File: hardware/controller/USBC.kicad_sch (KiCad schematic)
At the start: 8 parts

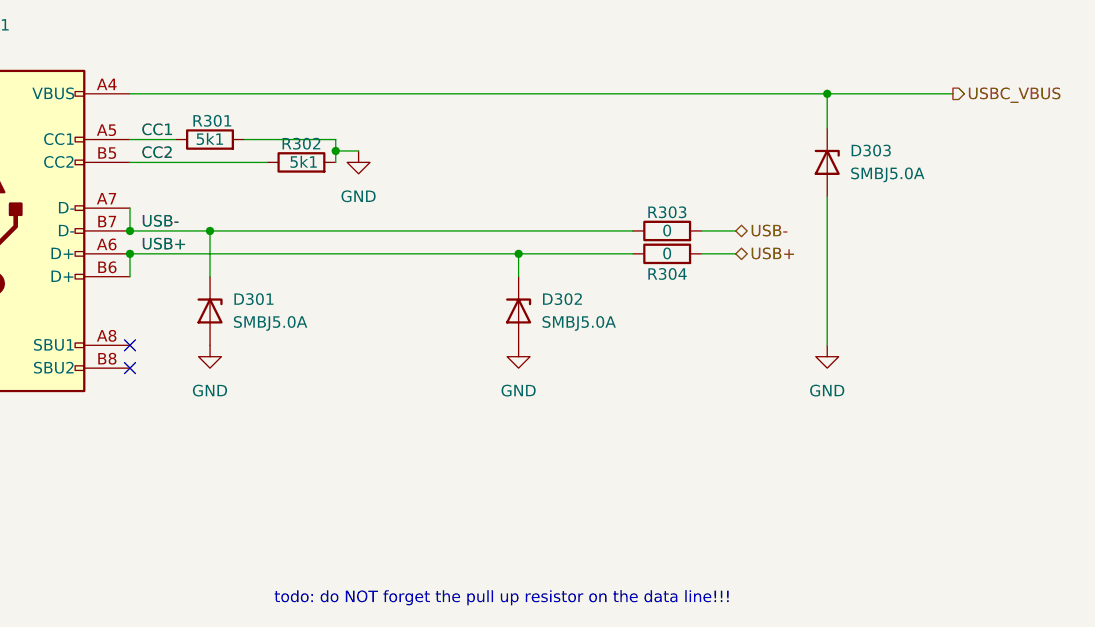
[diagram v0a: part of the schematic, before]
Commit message: fixed 3d models. rounded edges of pcb
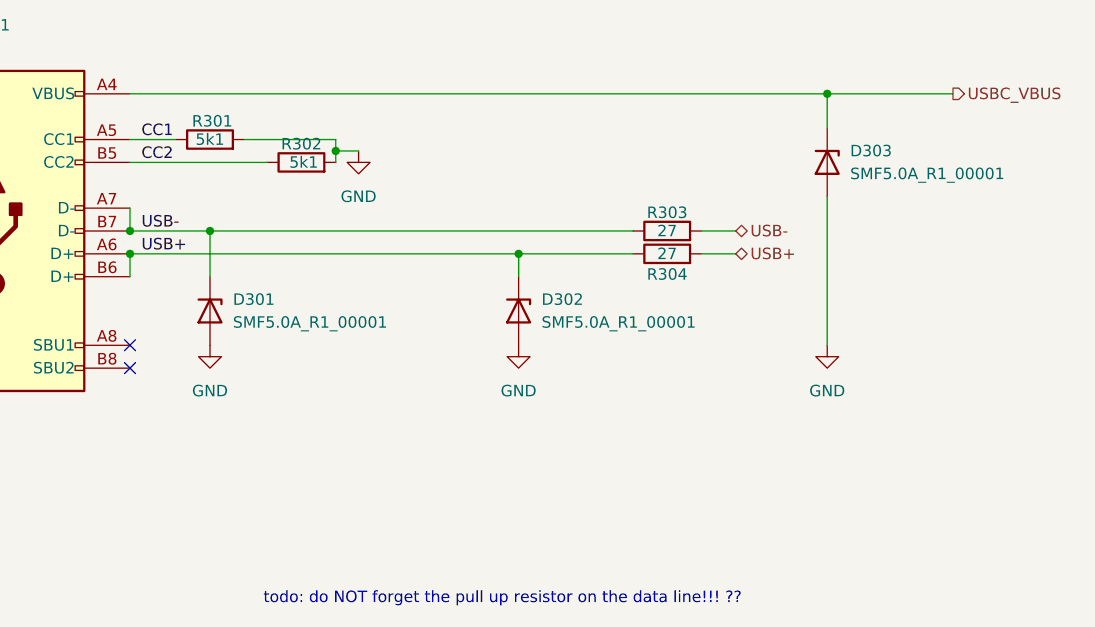
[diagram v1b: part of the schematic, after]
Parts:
- D301, D302, D303: value SMBJ5.0A -> SMF5.0A_R1_00001; footprint SamacSys_Parts:DIOM5436X261N -> SMF50A_R1_00001; Height 2.61 -> 1.1; Manufacturer_Name LITTELFUSE -> PANJIT; Manufacturer_Part_Number SMBJ5.0A -> SMF5.0A_R1_00001; Mouser Part Number 576-SMBJ5.0A -> 241-SMF5.0A_R1_00001; Mouser Price/Stock https://www.mouser.co.uk/ProductDetail/Littelfuse/SMBJ5.0A?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 -> https://www.mouser.co.uk/ProductDetail/Panjit/SMF5.0A_R1_00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
- R303, R304: value 0 -> 27; footprint SamacSys_Parts:RESC1608X50N -> RESC3216X65N; Height 0.5 -> 0.65; Manufacturer_Name Vishay -> ROHM Semiconductor; Manufacturer_Part_Number CRCW06030000Z0EA -> KTR18EZPF27R0; Mouser Part Number 71-CRCW0603-0-E3 -> 755-KTR18EZPF27R0; Mouser Price/Stock https://www.mouser.co.uk/ProductDetail/Vishay-Dale/CRCW0603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 -> https://www.mouser.com/Search/Refine.aspx?Keyword=755-KTR18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
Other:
- note added: "todo: do NOT forget the pull up resistor on the data line!!! ??"
- note removed: "todo: do NOT forget the pull up resistor on the data line!!!"
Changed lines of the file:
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@@
 	(generator_version "9.0")
 	(paper "A4")
-	(text "todo: do NOT forget the pull up resistor on the data line!!!"
+	(text "todo: do NOT forget the pull up resistor on the data line!!! ??"
 		(exclude_from_sim no)
 		(at 162.052 125.984 0)
@@
 			)
 		)
-		(property "Value" "SMBJ5.0A"
+		(property "Value" "SMF5.0A_R1_00001"
 			(at 166.37 95.2499 90)
 			(effects
@@
 			)
 		)
-		(property "Footprint" "SamacSys_Parts:DIOM5436X261N"
+		(property "Footprint" "SMF50A_R1_00001"
 			(at 70.18 104.14 0)
 			(effects
@@
 			)
 		)
-		(property "Datasheet" "https://www.mouser.co.uk/datasheet/2/240/Littelfuse_TVS_Diode_SMBJ_Datasheet.pdf-1108540.pdf"
+		(property "Datasheet" "https://www.mouser.in/datasheet/2/1057/SMF5.0A_SERIES-1868418.pdf"
 			(at -29.82 104.14 0)
 			(effects
@@
 			)
 		)
-		(property "Description" "Littelfuse SMBJ5.0A, Uni-Directional TVS Diode, 600W, 2-Pin DO-214AA"
+		(property "Description" "ESD Suppressors / TVS Diodes 200W,Transient Voltage Suppressors,SOD-123FL,5V,UNI"
 			(at 163.83 93.98 0)
 			(effects
@@
 			)
 		)
-		(property "Height" "2.61"
+		(property "Height" "1.1"
 			(at -229.82 104.14 0)
 			(effects
@@
 			)
 		)
-		(property "Mouser Part Number" "576-SMBJ5.0A"
+		(property "Mouser Part Number" "241-SMF5.0A_R1_00001"
 			(at -329.82 104.14 0)
 			(effects
@@
 			)
 		)
-		(property "Mouser Price/Stock" "https://www.mouser.co.uk/ProductDetail/Littelfuse/SMBJ5.0A?qs=JJML70Qc14t9tktzNr1oMQ%3D%3D"
+		(property "Mouser Price/Stock" "https://www.mouser.co.uk/ProductDetail/Panjit/SMF5.0A_R1_00001?qs=sPbYRqrBIVlx%2FHVv%252BUyL%252BQ%3D%3D"
 			(at -429.82 104.14 0)
 			(effects
@@
 			)
 		)
-		(property "Manufacturer_Name" "LITTELFUSE"
+		(property "Manufacturer_Name" "PANJIT"
 			(at -529.82 104.14 0)
 			(effects
@@
 			)
 		)
-		(property "Manufacturer_Part_Number" "SMBJ5.0A"
+		(property "Manufacturer_Part_Number" "SMF5.0A_R1_00001"
 			(at -629.82 104.14 0)
 			(effects
@@
 			)
 		)
-		(property "Value" "SMBJ5.0A"
+		(property "Value" "SMF5.0A_R1_00001"
 			(at 200.66 78.7399 90)
 			(effects
@@
 			)
 		)
-		(property "Footprint" "SamacSys_Parts:DIOM5436X261N"
+		(property "Footprint" "SMF50A_R1_00001"
 			(at 104.47 87.63 0)
 			(effects
@@
 			)
 		)
-		(property "Datasheet" "https://www.mouser.co.uk/datasheet/2/240/Littelfuse_TVS_Diode_SMBJ_Datasheet.pdf-1108540.pdf"
+		(property "Datasheet" "https://www.mouser.in/datasheet/2/1057/SMF5.0A_SERIES-1868418.pdf"
 			(at 4.47 87.63 0)
 			(effects
@@
 			)
 		)
-		(property "Description" "Littelfuse SMBJ5.0A, Uni-Directional TVS Diode, 600W, 2-Pin DO-214AA"
+		(property "Description" "ESD Suppressors / TVS Diodes 200W,Transient Voltage Suppressors,SOD-123FL,5V,UNI"
 			(at 198.12 77.47 0)
 			(effects
@@
 			)
 		)
-		(property "Height" "2.61"
+		(property "Height" "1.1"
 			(at -195.53 87.63 0)
 			(effects
@@
 			)
 		)
-		(property "Mouser Part Number" "576-SMBJ5.0A"
+		(property "Mouser Part Number" "241-SMF5.0A_R1_00001"
 			(at -295.53 87.63 0)
 			(effects
@@
 			)
 		)
-		(property "Mouser Price/Stock" "https://www.mouser.co.uk/ProductDetail/Littelfuse/SMBJ5.0A?qs=JJML70Qc14t9tktzNr1oMQ%3D%3D"
+		(property "Mouser Price/Stock" "https://www.mouser.co.uk/ProductDetail/Panjit/SMF5.0A_R1_00001?qs=sPbYRqrBIVlx%2FHVv%252BUyL%252BQ%3D%3D"
 			(at -395.53 87.63 0)
 			(effects
@@
 			)
 		)
-		(property "Manufacturer_Name" "LITTELFUSE"
+		(property "Manufacturer_Name" "PANJIT"
 			(at -495.53 87.63 0)
 			(effects
@@
 			)
 		)
-		(property "Manufacturer_Part_Number" "SMBJ5.0A"
+		(property "Manufacturer_Part_Number" "SMF5.0A_R1_00001"
 			(at -595.53 87.63 0)
 			(effects
@@
 			)
 		)
-		(property "Value" "0"
+		(property "Value" "27"
 			(at 180.34 87.63 90)
 			(effects
@@
 			)
 		)
-		(property "Footprint" "SamacSys_Parts:RESC1608X50N"
+		(property "Footprint" "RESC3216X65N"
 			(at 276.53 73.66 0)
 			(effects
@@
 			)
 		)
-		(property "Datasheet" "http://www.vishay.com/docs/20035/dcrcwe3.pdf"
+		(property "Datasheet" "https://componentsearchengine.com/Datasheets/1/KTR18EZPF27R0.pdf"
 			(at 376.53 73.66 0)
 			(effects
@@
 			)
 		)
-		(property "Description" "VISHAY - CRCW06030000Z0EA - RESISTOR, 0R, 0.1W, JUMPER, 0603, SMD"
+		(property "Description" "Thick Film Resistors - SMD 1206 27ohm 1% High VoltageAEC-Q200"
 			(at 180.34 87.63 0)
 			(effects
@@
 			)
 		)
-		(property "Height" "0.5"
+		(property "Height" "0.65"
 			(at 576.53 73.66 0)
 			(effects
@@
 			)
 		)
-		(property "Mouser Part Number" "71-CRCW0603-0-E3"
+		(property "Mouser Part Number" "755-KTR18EZPF27R0"
 			(at 676.53 73.66 0)
 			(effects
@@
 			)
 		)
-		(property "Mouser Price/Stock" "https://www.mouser.co.uk/ProductDetail/Vishay-Dale/CRCW06030000Z0EA?qs=uFJqmf%2F3rbbVtxvMdbYUaQ%3D%3D"
+		(property "Mouser Price/Stock" "https://www.mouser.com/Search/Refine.aspx?Keyword=755-KTR18EZPF27R0"
 			(at 776.53 73.66 0)
 			(effects
@@
 			)
 		)
-		(property "Manufacturer_Name" "Vishay"
+		(property "Manufacturer_Name" "ROHM Semiconductor"
 			(at 876.53 73.66 0)
 			(effects
@@
 			)
 		)
-		(property "Manufacturer_Part_Number" "CRCW06030000Z0EA"
+		(property "Manufacturer_Part_Number" "KTR18EZPF27R0"
 			(at 976.53 73.66 0)
 			(effects
@@
 			)
 		)
-		(property "Value" "SMBJ5.0A"
+		(property "Value" "SMF5.0A_R1_00001"
 			(at 132.08 95.2499 90)
 			(effects
@@
 			)
 		)
-		(property "Footprint" "SamacSys_Parts:DIOM5436X261N"
+		(property "Footprint" "SMF50A_R1_00001"
 			(at 35.89 104.14 0)
 			(effects
@@
 			)
 		)
-		(property "Datasheet" "https://www.mouser.co.uk/datasheet/2/240/Littelfuse_TVS_Diode_SMBJ_Datasheet.pdf-1108540.pdf"
+		(property "Datasheet" "https://www.mouser.in/datasheet/2/1057/SMF5.0A_SERIES-1868418.pdf"
 			(at -64.11 104.14 0)
 			(effects
@@
 			)
 		)
-		(property "Description" "Littelfuse SMBJ5.0A, Uni-Directional TVS Diode, 600W, 2-Pin DO-214AA"
+		(property "Description" "ESD Suppressors / TVS Diodes 200W,Transient Voltage Suppressors,SOD-123FL,5V,UNI"
 			(at 129.54 93.98 0)
 			(effects
@@
 			)
 		)
-		(property "Height" "2.61"
+		(property "Height" "1.1"
 			(at -264.11 104.14 0)
 			(effects
@@
 			)
 		)
-		(property "Mouser Part Number" "576-SMBJ5.0A"
+		(property "Mouser Part Number" "241-SMF5.0A_R1_00001"
 			(at -364.11 104.14 0)
 			(effects
@@
 			)
 		)
-		(property "Mouser Price/Stock" "https://www.mouser.co.uk/ProductDetail/Littelfuse/SMBJ5.0A?qs=JJML70Qc14t9tktzNr1oMQ%3D%3D"
+		(property "Mouser Price/Stock" "https://www.mouser.co.uk/ProductDetail/Panjit/SMF5.0A_R1_00001?qs=sPbYRqrBIVlx%2FHVv%252BUyL%252BQ%3D%3D"
 			(at -464.11 104.14 0)
 			(effects
@@
 			)
 		)
-		(property "Manufacturer_Name" "LITTELFUSE"
+		(property "Manufacturer_Name" "PANJIT"
 			(at -564.11 104.14 0)
 			(effects
@@
 			)
 		)
-		(property "Manufacturer_Part_Number" "SMBJ5.0A"
+		(property "Manufacturer_Part_Number" "SMF5.0A_R1_00001"
 			(at -664.11 104.14 0)
 			(effects
@@
 			)
 		)
-		(property "Value" "0"
+		(property "Value" "27"
 			(at 180.34 85.09 90)
 			(effects
@@
 			)
 		)
-		(property "Footprint" "SamacSys_Parts:RESC1608X50N"
+		(property "Footprint" "RESC3216X65N"
 			(at 276.53 71.12 0)
 			(effects
@@
 			)
 		)
-		(property "Datasheet" "http://www.vishay.com/docs/20035/dcrcwe3.pdf"
+		(property "Datasheet" "https://componentsearchengine.com/Datasheets/1/KTR18EZPF27R0.pdf"
 			(at 376.53 71.12 0)
 			(effects
@@
 			)
 		)
-		(property "Description" "VISHAY - CRCW06030000Z0EA - RESISTOR, 0R, 0.1W, JUMPER, 0603, SMD"
+		(property "Description" "Thick Film Resistors - SMD 1206 27ohm 1% High VoltageAEC-Q200"
 			(at 180.34 85.09 0)
 			(effects
@@
 			)
 		)
-		(property "Height" "0.5"
+		(property "Height" "0.65"
 			(at 576.53 71.12 0)
 			(effects
@@
 			)
 		)
-		(property "Mouser Part Number" "71-CRCW0603-0-E3"
+		(property "Mouser Part Number" "755-KTR18EZPF27R0"
 			(at 676.53 71.12 0)
 			(effects
@@
 			)
 		)
-		(property "Mouser Price/Stock" "https://www.mouser.co.uk/ProductDetail/Vishay-Dale/CRCW06030000Z0EA?qs=uFJqmf%2F3rbbVtxvMdbYUaQ%3D%3D"
+		(property "Mouser Price/Stock" "https://www.mouser.com/Search/Refine.aspx?Keyword=755-KTR18EZPF27R0"
 			(at 776.53 71.12 0)
 			(effects
@@
 			)
 		)
-		(property "Manufacturer_Name" "Vishay"
+		(property "Manufacturer_Name" "ROHM Semiconductor"
 			(at 876.53 71.12 0)
 			(effects
@@
 			)
 		)
-		(property "Manufacturer_Part_Number" "CRCW06030000Z0EA"
+		(property "Manufacturer_Part_Number" "KTR18EZPF27R0"
 			(at 976.53 71.12 0)
 			(effects

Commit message: man im tired
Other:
- note added: "todo: find smaller resistors that have pads to fit right into the USB data tracks"
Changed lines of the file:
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@@
+		)
+	)
+	(text "todo: find smaller resistors that have pads to fit right into\nthe USB data tracks"
+		(exclude_from_sim no)
+		(at 178.054 79.502 0)
+		(effects
+			(font
+				(size 1.27 1.27)
+			)
 		)
 	)

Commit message: a
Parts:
- D301, D302, D303: footprint SMF50A_R1_00001 -> SamacSys_Parts:SMF50A_R1_00001
- R303, R304: footprint RESC3216X65N -> SamacSys_Parts:RESC1005X40N; Height 0.65 -> 0.4; Manufacturer_Name ROHM Semiconductor -> Vishay; Manufacturer_Part_Number KTR18EZPF27R0 -> CRCW040227R0JNTD; Mouser Part Number 755-KTR18EZPF27R0 -> 71-CRCW0402J-27; Mouser Price/Stock https://www.mouser.com/Search/Refine.aspx?Keyword=755-KTR18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 -> https://www.mouser.com/Search/Refine.aspx?Keyword=71-CRCW04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
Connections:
- net USB+: no longer D302.1 (K), J301.A6 (D+), J301.B6 (D+), R304.1
- net USB-: no longer D301.1 (K), J301.A7 (D-), J301.B7 (D-), R303.1
- new net D+: D302.1 (K), J301.A6 (D+), J301.B6 (D+), R304.1
- new net D-: D301.1 (K), J301.A7 (D-), J301.B7 (D-), R303.1
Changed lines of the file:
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@@
 		)
 	)
-	(label "USB+"
+	(label "D+"
 		(at 121.92 87.63 0)
 		(effects
@@
 		)
 	)
-	(label "USB-"
+	(label "D-"
 		(at 121.92 85.09 0)
 		(effects
@@
 			)
 		)
-		(property "Footprint" "SMF50A_R1_00001"
+		(property "Footprint" "SamacSys_Parts:SMF50A_R1_00001"
 			(at 70.18 104.14 0)
 			(effects
@@
 			)
 		)
-		(property "Footprint" "SMF50A_R1_00001"
+		(property "Footprint" "SamacSys_Parts:SMF50A_R1_00001"
 			(at 104.47 87.63 0)
 			(effects
@@
 			)
 		)
-		(property "Footprint" "RESC3216X65N"
+		(property "Footprint" "SamacSys_Parts:RESC1005X40N"
 			(at 276.53 73.66 0)
 			(effects
@@
 			)
 		)
-		(property "Datasheet" "https://componentsearchengine.com/Datasheets/1/KTR18EZPF27R0.pdf"
+		(property "Datasheet" "https://componentsearchengine.com/Datasheets/1/CRCW040227R0JNTD.pdf"
 			(at 376.53 73.66 0)
 			(effects
@@
 			)
 		)
-		(property "Description" "Thick Film Resistors - SMD 1206 27ohm 1% High VoltageAEC-Q200"
+		(property "Description" "Thick Film Resistors - SMD 1/16watt 27ohms 5%"
 			(at 180.34 87.63 0)
 			(effects
@@
 			)
 		)
-		(property "Height" "0.65"
+		(property "Height" "0.4"
 			(at 576.53 73.66 0)
 			(effects
@@
 			)
 		)
-		(property "Mouser Part Number" "755-KTR18EZPF27R0"
+		(property "Mouser Part Number" "71-CRCW0402J-27"
 			(at 676.53 73.66 0)
 			(effects
@@
 			)
 		)
-		(property "Mouser Price/Stock" "https://www.mouser.com/Search/Refine.aspx?Keyword=755-KTR18EZPF27R0"
+		(property "Mouser Price/Stock" "https://www.mouser.com/Search/Refine.aspx?Keyword=71-CRCW0402J-27"
 			(at 776.53 73.66 0)
 			(effects
@@
 			)
 		)
-		(property "Manufacturer_Name" "ROHM Semiconductor"
+		(property "Manufacturer_Name" "Vishay"
 			(at 876.53 73.66 0)
 			(effects
@@
 			)
 		)
-		(property "Manufacturer_Part_Number" "KTR18EZPF27R0"
+		(property "Manufacturer_Part_Number" "CRCW040227R0JNTD"
 			(at 976.53 73.66 0)
 			(effects
@@
 			)
 		)
-		(property "Footprint" "SMF50A_R1_00001"
+		(property "Footprint" "SamacSys_Parts:SMF50A_R1_00001"
 			(at 35.89 104.14 0)
 			(effects
@@
 			)
 		)
-		(property "Footprint" "RESC3216X65N"
+		(property "Footprint" "SamacSys_Parts:RESC1005X40N"
 			(at 276.53 71.12 0)
 			(effects
@@
 			)
 		)
-		(property "Datasheet" "https://componentsearchengine.com/Datasheets/1/KTR18EZPF27R0.pdf"
+		(property "Datasheet" "https://componentsearchengine.com/Datasheets/1/CRCW040227R0JNTD.pdf"
 			(at 376.53 71.12 0)
 			(effects
@@
 			)
 		)
-		(property "Description" "Thick Film Resistors - SMD 1206 27ohm 1% High VoltageAEC-Q200"
+		(property "Description" "Thick Film Resistors - SMD 1/16watt 27ohms 5%"
 			(at 180.34 85.09 0)
 			(effects
@@
 			)
 		)
-		(property "Height" "0.65"
+		(property "Height" "0.4"
 			(at 576.53 71.12 0)
 			(effects
@@
 			)
 		)
-		(property "Mouser Part Number" "755-KTR18EZPF27R0"
+		(property "Mouser Part Number" "71-CRCW0402J-27"
 			(at 676.53 71.12 0)
 			(effects
@@
 			)
 		)
-		(property "Mouser Price/Stock" "https://www.mouser.com/Search/Refine.aspx?Keyword=755-KTR18EZPF27R0"
+		(property "Mouser Price/Stock" "https://www.mouser.com/Search/Refine.aspx?Keyword=71-CRCW0402J-27"
 			(at 776.53 71.12 0)
 			(effects
@@
 			)
 		)
-		(property "Manufacturer_Name" "ROHM Semiconductor"
+		(property "Manufacturer_Name" "Vishay"
 			(at 876.53 71.12 0)
 			(effects
@@
 			)
 		)
-		(property "Manufacturer_Part_Number" "KTR18EZPF27R0"
+		(property "Manufacturer_Part_Number" "CRCW040227R0JNTD"
 			(at 976.53 71.12 0)
 			(effects

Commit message: save before nuke
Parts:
- renumbered D301 to D104, D302 to D105, D303 to D106, J301 to J102, R301 to R104, R302 to R105, R303 to R106, R304 to R107
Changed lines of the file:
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@@
 		(dnp no)
 		(fields_autoplaced yes)
-		(property "Reference" "J301"
+		(property "Reference" "J102"
 			(at 105.41 62.23 0)
 			(effects
@@
 			(project ""
 				(path "/869bea87-c885-4ead-826b-3f34ceacafad/26d17bc2-e2ae-44e6-8fc3-d458d6e51b4a"
-					(reference "J301")
+					(reference "J102")
 					(unit 1)
 				)
@@
 		(dnp no)
 		(fields_autoplaced yes)
-		(property "Reference" "#PWR0301"
+		(property "Reference" "#PWR0121"
 			(at 97.79 120.65 0)
 			(effects
@@
 			(project ""
 				(path "/869bea87-c885-4ead-826b-3f34ceacafad/26d17bc2-e2ae-44e6-8fc3-d458d6e51b4a"
-					(reference "#PWR0301")
+					(reference "#PWR0121")
 					(unit 1)
 				)
@@
 		(dnp no)
 		(fields_autoplaced yes)
-		(property "Reference" "#PWR0303"
+		(property "Reference" "#PWR0123"
 			(at 146.05 82.55 0)
 			(effects
@@
 			(project ""
 				(path "/869bea87-c885-4ead-826b-3f34ceacafad/26d17bc2-e2ae-44e6-8fc3-d458d6e51b4a"
-					(reference "#PWR0303")
+					(reference "#PWR0123")
 					(unit 1)
 				)
@@
 		(dnp no)
 		(fields_autoplaced yes)
-		(property "Reference" "D302"
+		(property "Reference" "D105"
 			(at 166.37 92.7099 90)
 			(effects
@@
 			(project "controller"
 				(path "/869bea87-c885-4ead-826b-3f34ceacafad/26d17bc2-e2ae-44e6-8fc3-d458d6e51b4a"
-					(reference "D302")
+					(reference "D105")
 					(unit 1)
 				)
@@
 		(on_board yes)
 		(dnp no)
-		(property "Reference" "R301"
+		(property "Reference" "R104"
 			(at 129.794 72.898 90)
 			(effects
@@
 			(project ""
 				(path "/869bea87-c885-4ead-826b-3f34ceacafad/26d17bc2-e2ae-44e6-8fc3-d458d6e51b4a"
-					(reference "R301")
+					(reference "R104")
 					(unit 1)
 				)
@@
 		(dnp no)
 		(fields_autoplaced yes)
-		(property "Reference" "D303"
+		(property "Reference" "D106"
 			(at 200.66 76.1999 90)
 			(effects
@@
 			(project "controller"
 				(path "/869bea87-c885-4ead-826b-3f34ceacafad/26d17bc2-e2ae-44e6-8fc3-d458d6e51b4a"
-					(reference "D303")
+					(reference "D106")
 					(unit 1)
 				)
@@
 		(dnp no)
 		(fields_autoplaced yes)
-		(property "Reference" "#PWR0304"
+		(property "Reference" "#PWR0124"
 			(at 163.83 104.14 0)
 			(effects
@@
 			(project "controller"
 				(path "/869bea87-c885-4ead-826b-3f34ceacafad/26d17bc2-e2ae-44e6-8fc3-d458d6e51b4a"
-					(reference "#PWR0304")
+					(reference "#PWR0124")
 					(unit 1)
 				)
@@
 		(dnp no)
 		(fields_autoplaced yes)
-		(property "Reference" "#PWR0305"
+		(property "Reference" "#PWR0125"
 			(at 198.12 104.14 0)
 			(effects
@@
 			(project ""
 				(path "/869bea87-c885-4ead-826b-3f34ceacafad/26d17bc2-e2ae-44e6-8fc3-d458d6e51b4a"
-					(reference "#PWR0305")
+					(reference "#PWR0125")
 					(unit 1)
 				)
@@
 		(on_board yes)
 		(dnp no)
-		(property "Reference" "R304"
+		(property "Reference" "R107"
 			(at 180.34 89.916 90)
 			(effects
@@
 			(project "controller"
 				(path "/869bea87-c885-4ead-826b-3f34ceacafad/26d17bc2-e2ae-44e6-8fc3-d458d6e51b4a"
-					(reference "R304")
+					(reference "R107")
 					(unit 1)
 				)
@@
 		(dnp no)
 		(fields_autoplaced yes)
-		(property "Reference" "D301"
+		(property "Reference" "D104"
 			(at 132.08 92.7099 90)
 			(effects
@@
 			(project "controller"
 				(path "/869bea87-c885-4ead-826b-3f34ceacafad/26d17bc2-e2ae-44e6-8fc3-d458d6e51b4a"
-					(reference "D301")
+					(reference "D104")
 					(unit 1)
 				)
@@
 		(on_board yes)
 		(dnp no)
-		(property "Reference" "R303"
+		(property "Reference" "R106"
 			(at 180.34 83.058 90)
 			(effects
@@
 			(project ""
 				(path "/869bea87-c885-4ead-826b-3f34ceacafad/26d17bc2-e2ae-44e6-8fc3-d458d6e51b4a"
-					(reference "R303")
+					(reference "R106")
 					(unit 1)
 				)
@@
 		(on_board yes)
 		(dnp no)
-		(property "Reference" "R302"
+		(property "Reference" "R105"
 			(at 139.7 75.438 90)
 			(effects
@@
 			(project "controller"
 				(path "/869bea87-c885-4ead-826b-3f34ceacafad/26d17bc2-e2ae-44e6-8fc3-d458d6e51b4a"
-					(reference "R302")
+					(reference "R105")
 					(unit 1)
 				)
@@
 		(dnp no)
 		(fields_autoplaced yes)
-		(property "Reference" "#PWR0302"
+		(property "Reference" "#PWR0122"
 			(at 129.54 104.14 0)
 			(effects
@@
 			(project "controller"
 				(path "/869bea87-c885-4ead-826b-3f34ceacafad/26d17bc2-e2ae-44e6-8fc3-d458d6e51b4a"
-					(reference "#PWR0302")
+					(reference "#PWR0122")
 					(unit 1)
 				)

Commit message: forgor
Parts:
- J102: footprint SamacSys_Parts:USB_C_Receptacle_GCT_USB4105-xx-A_16P_TopMnt_Horizontal -> SamacSys_Parts:USB480003A; Height (none) -> 5.58; Manufacturer_Name (none) -> GCT (GLOBAL CONNECTOR TECHNOLOGY); Manufacturer_Part_Number (none) -> USB4800-03-A; Mouser Part Number (none) -> 640-USB4800-03-A; Mouser Price/Stock (none) -> https://www.mouser.co.uk/ProductDetail/GCT/USB4800-03-A?qs=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
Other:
- note added: "Hierarchical Pins"
- note added: "USB"
- note added: "todo: check if need pull up resistor on data lines"
- note removed: "todo: do NOT forget the pull up resistor on the data line!!! ??"
- note removed: "todo: find smaller resistors that have pads to fit right into the USB data tracks"
- moved on the sheet: D104, D105, D106, J102, R104, R105, R106, R107
